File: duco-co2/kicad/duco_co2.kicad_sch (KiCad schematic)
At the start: 1 part, among them X1 S8B-PH-K-S 8

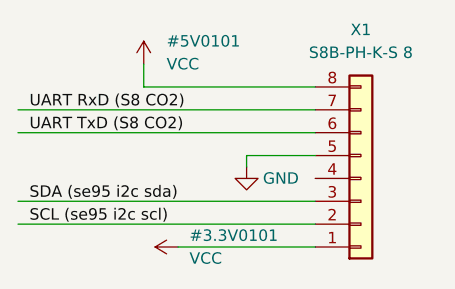
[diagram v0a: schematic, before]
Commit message: fixed VCC by using power ports
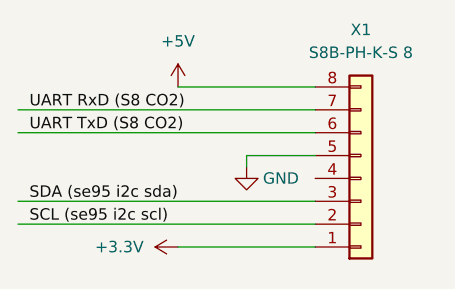
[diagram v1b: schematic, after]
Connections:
- net VCC renamed +3V3
- net +3V3: no longer X1.8 (Pin_8)
- new net +5V: X1.8 (Pin_8)
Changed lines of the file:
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@@
-    (stroke (width 0) (type default) (color 0 0 0 0))
-  )
-  (wire (pts (xy 64.77 58.42) (xy 64.77 55.88))
     (stroke (width 0) (type default) (color 0 0 0 0))
   )
@@
     (stroke (width 0) (type default) (color 0 0 0 0))
   )
-  (wire (pts (xy 64.77 58.42) (xy 83.82 58.42))
+  (wire (pts (xy 68.58 58.42) (xy 83.82 58.42))
     (stroke (width 0) (type default) (color 0 0 0 0))
   )
@@
     (effects (font (size 1.27 1.27)) (justify left bottom))
   )
-  (symbol (lib_id "power:VCC") (at 64.77 55.88 0) (unit 1)
+  (symbol (lib_id "power:+5V") (at 68.58 58.42 0) (unit 1)
     (in_bom yes) (on_board yes) (fields_autoplaced)
-    (property "Reference" "#5V0101" (id 0) (at 67.31 53.3399 0)
-      (effects (font (size 1.27 1.27)) (justify left))
-    )
-    (property "Value" "VCC" (id 1) (at 67.31 55.8799 0)
-      (effects (font (size 1.27 1.27)) (justify left))
-    )
-    (property "Footprint" "" (id 2) (at 64.77 55.88 0)
+    (property "Reference" "#PWR?" (id 0) (at 68.58 62.23 0)
       (effects (font (size 1.27 1.27)) hide)
     )
-    (property "Datasheet" "" (id 3) (at 64.77 55.88 0)
+    (property "Value" "+5V" (id 1) (at 68.58 53.34 0))
+    (property "Footprint" "" (id 2) (at 68.58 58.42 0)
+      (effects (font (size 1.27 1.27)) hide)
+    )
+    (property "Datasheet" "" (id 3) (at 68.58 58.42 0)
       (effects (font (size 1.27 1.27)) hide)
     )
@@
     (pin "8")
   )
-  (symbol (lib_id "power:VCC") (at 68.58 76.2 90) (unit 1)
-    (in_bom yes) (on_board yes) (fields_autoplaced)
-    (property "Reference" "#3.3V0101" (id 0) (at 69.85 74.9299 90)
-      (effects (font (size 1.27 1.27)) (justify right))
-    )
-    (property "Value" "VCC" (id 1) (at 69.85 77.4699 90)
-      (effects (font (size 1.27 1.27)) (justify right))
-    )
-    (property "Footprint" "" (id 2) (at 68.58 76.2 0)
-      (effects (font (size 1.27 1.27)) hide)
-    )
-    (property "Datasheet" "" (id 3) (at 68.58 76.2 0)
-      (effects (font (size 1.27 1.27)) hide)
-    )
-    (pin "1")
-  )
   (symbol (lib_id "power:GND") (at 76.2 67.31 0) (unit 1)
     (in_bom yes) (on_board yes)
@@
     (pin "1")
   )
+  (symbol (lib_id "power:+3.3V") (at 68.58 76.2 90) (unit 1)
+    (in_bom yes) (on_board yes) (fields_autoplaced)
+    (property "Reference" "#PWR?" (id 0) (at 72.39 76.2 0)
+      (effects (font (size 1.27 1.27)) hide)
+    )
+    (property "Value" "+3.3V" (id 1) (at 64.77 76.1999 90)
+      (effects (font (size 1.27 1.27)) (justify left))
+    )
+    (property "Footprint" "" (id 2) (at 68.58 76.2 0)
+      (effects (font (size 1.27 1.27)) hide)
+    )
+    (property "Datasheet" "" (id 3) (at 68.58 76.2 0)
+      (effects (font (size 1.27 1.27)) hide)
+    )
+    (pin "1")
+  )
   (sheet_instances
     (path "/" (page "1"))
   )
   (symbol_instances
-    (path "/b67c92c8-8960-4c22-a8b2-2c01374413c2"
-      (reference "#3.3V0101") (unit 1) (value "VCC") (footprint "")
-    )
-    (path "/38aaf2b1-3bf7-4863-b743-c3863a3a99ca"
-      (reference "#5V0101") (unit 1) (value "VCC") (footprint "")
-    )
     (path "/dd1b2aa3-e4a6-4e1f-ae6b-604f6f803358"
       (reference "#PWR0101") (unit 1) (value "GND") (footprint "")
     )
+    (path "/52e1058a-a84e-40ec-b420-1423f0d28a75"
+      (reference "#PWR?") (unit 1) (value "+5V") (footprint "")
+    )
+    (path "/ee202a96-96ee-464e-a148-4b76788af37e"
+      (reference "#PWR?") (unit 1) (value "+3.3V") (footprint "")
+    )
     (path "/57c8f3a1-debc-47be-9fca-9386eebd5d18"
